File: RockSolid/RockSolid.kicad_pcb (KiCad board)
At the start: 2 copper layers, 47 x 50.8 mm, 26 parts, among them J1 Conn_01x04, Q1 IRF510, U1 L78L05_TO92, U2 74HC04, Y1 10 Mhz

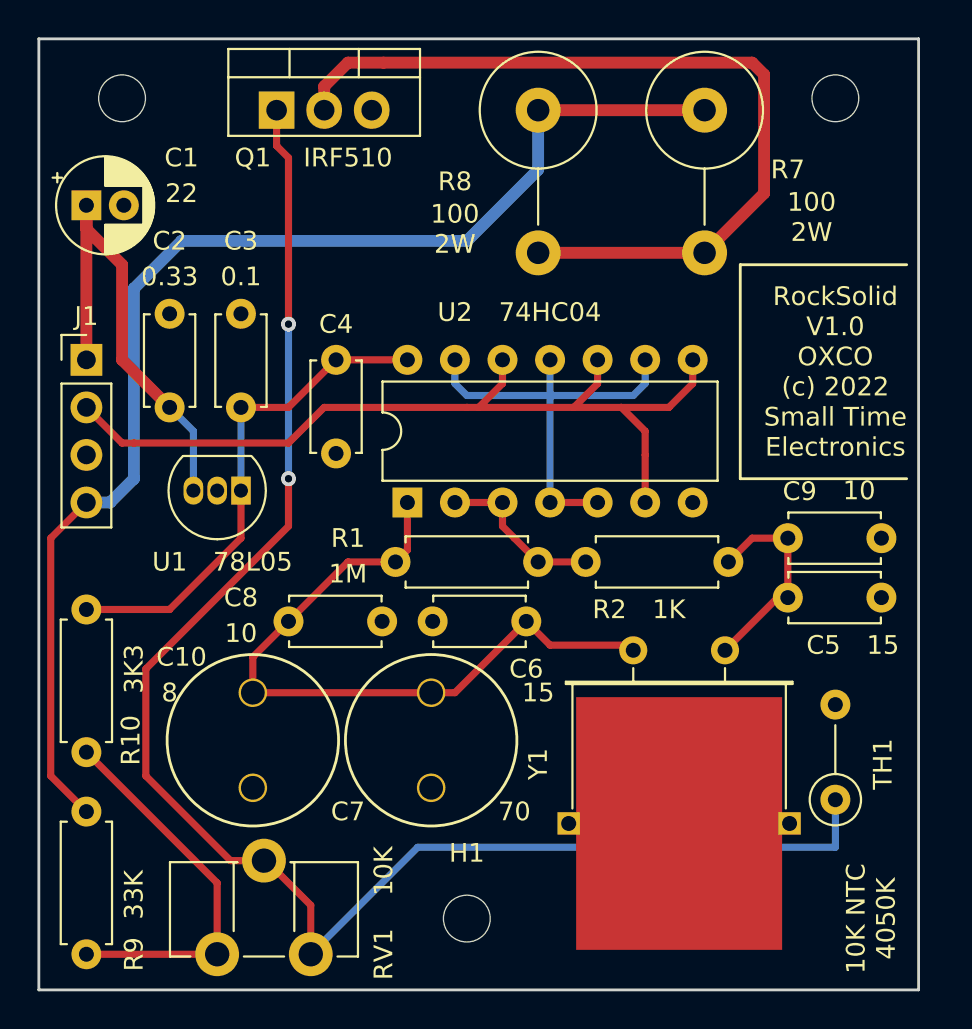
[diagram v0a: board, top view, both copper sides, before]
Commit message: v1.01 added labels on PCB, grounded crystal, silkscreen updates.
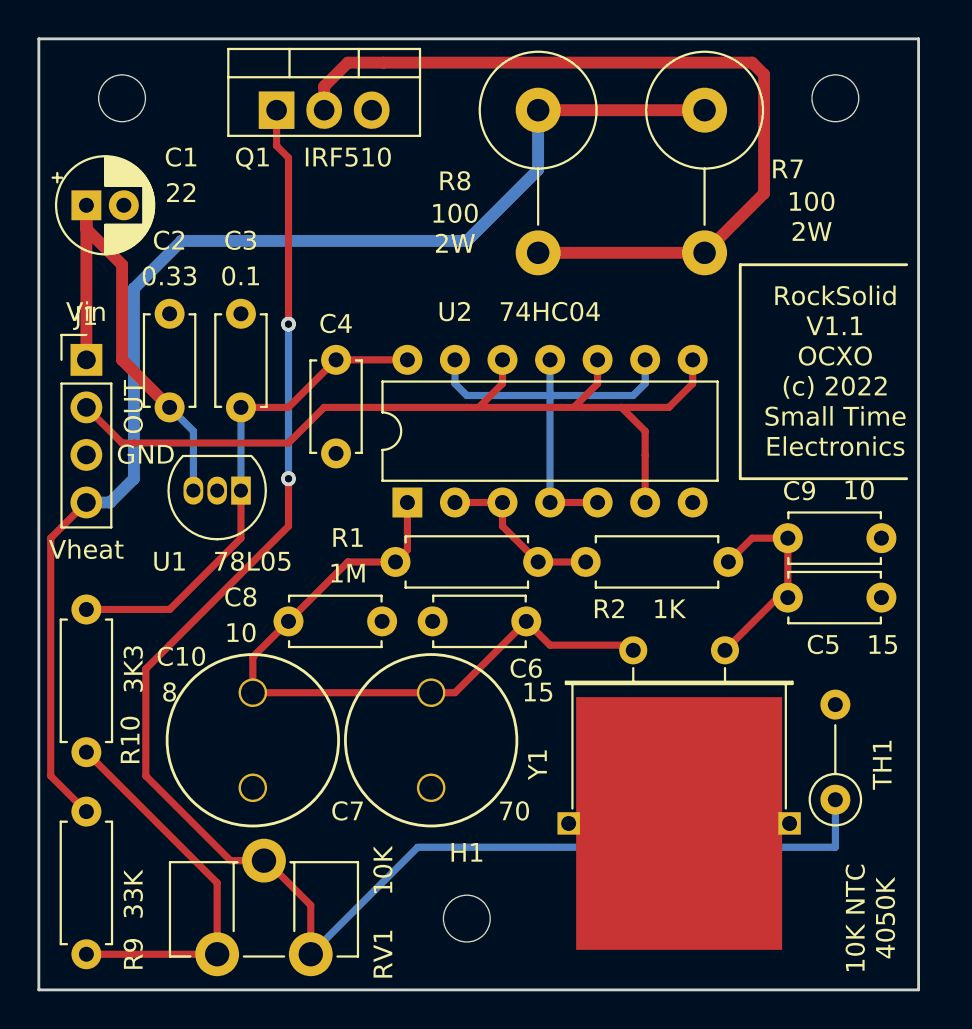
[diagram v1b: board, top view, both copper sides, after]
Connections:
- Y1 pad 3: Net-(Y1-Pad3) -> GND
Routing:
- net Net-(Y1-Pad3): track 17.5 -> 0.00 mm
- net GND: track 0.00 -> 17.5 mm
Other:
- board text added: "GND"
- board text added: "OUT"
- board text added: "Rock Solid OCXO (c) 2022 Will Cooke"
- board text added: "RockSolid V1.1 OCXO (c) 2022 Small Time Electronics"
- board text added: "Vheat"
- board text added: "Vin"
- board text added: "smalltimeelectronics.com"
- board text removed: "Rock Solid OCXO (c) 2021 Will Cooke smalltimeelectronics.com"
- board text removed: "RockSolid V1.0 OXCO (c) 2022 Small Time Electronics"
